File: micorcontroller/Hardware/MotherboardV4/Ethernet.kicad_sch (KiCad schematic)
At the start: 41 parts, among them IC2 W5500, J3 J1B1211CCD, Y1 ECS-250-6-33B2-CTP-TR

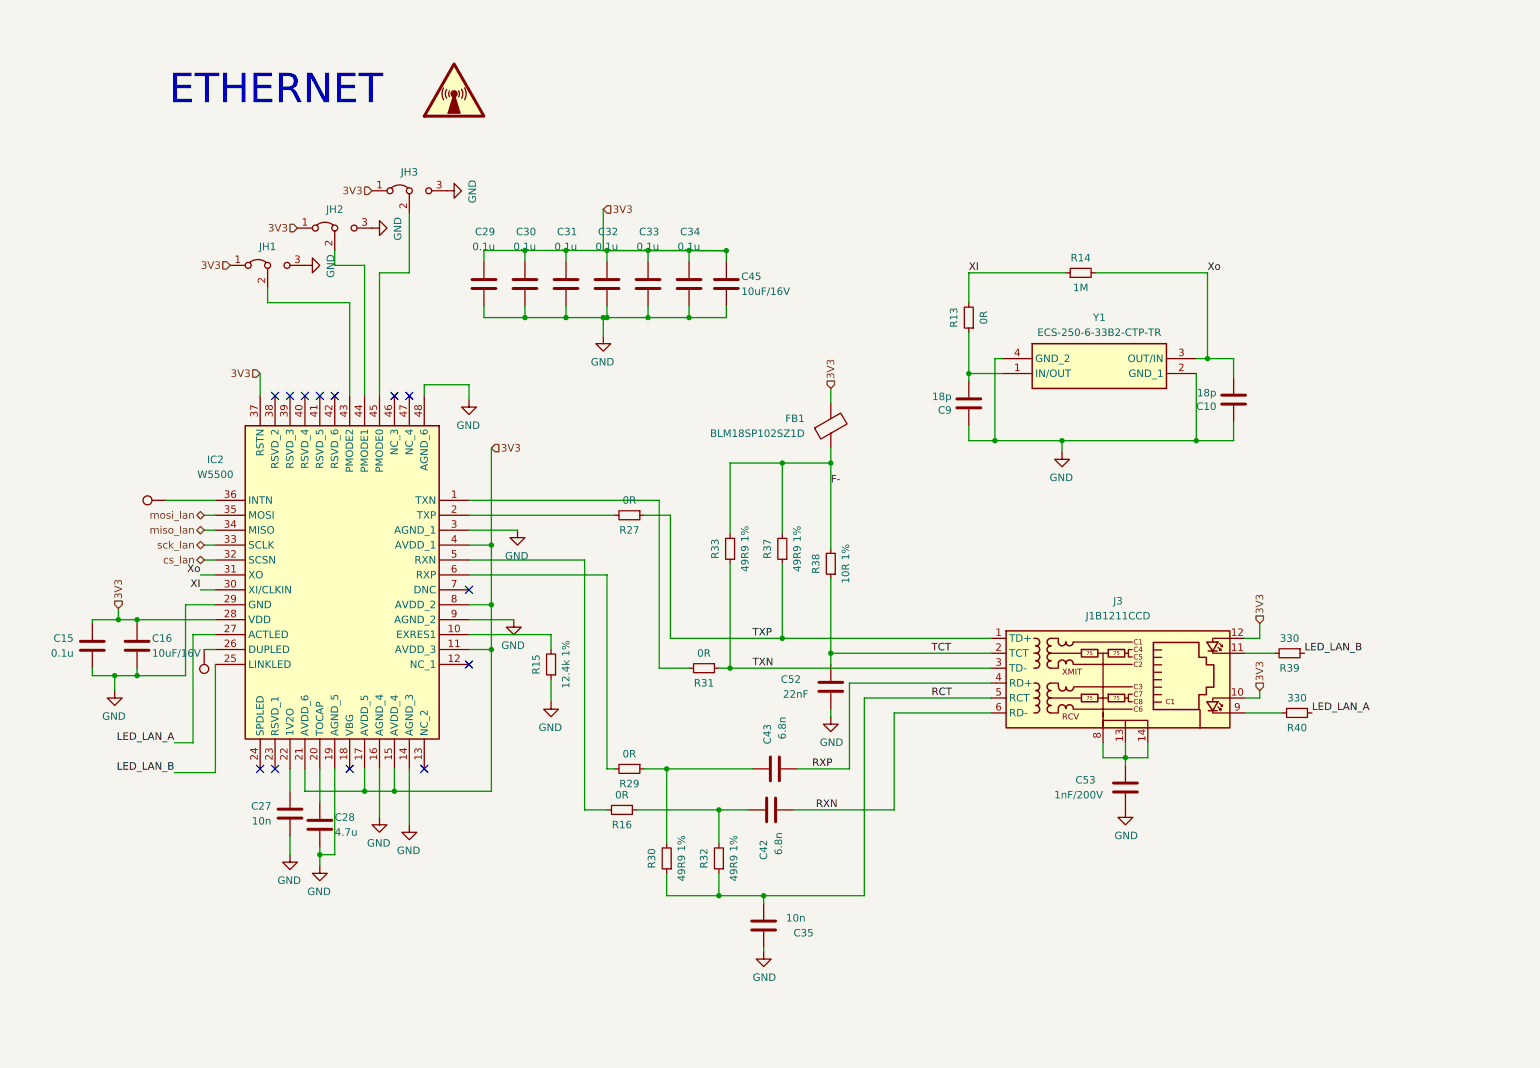
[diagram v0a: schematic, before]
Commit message: added NTC calculation
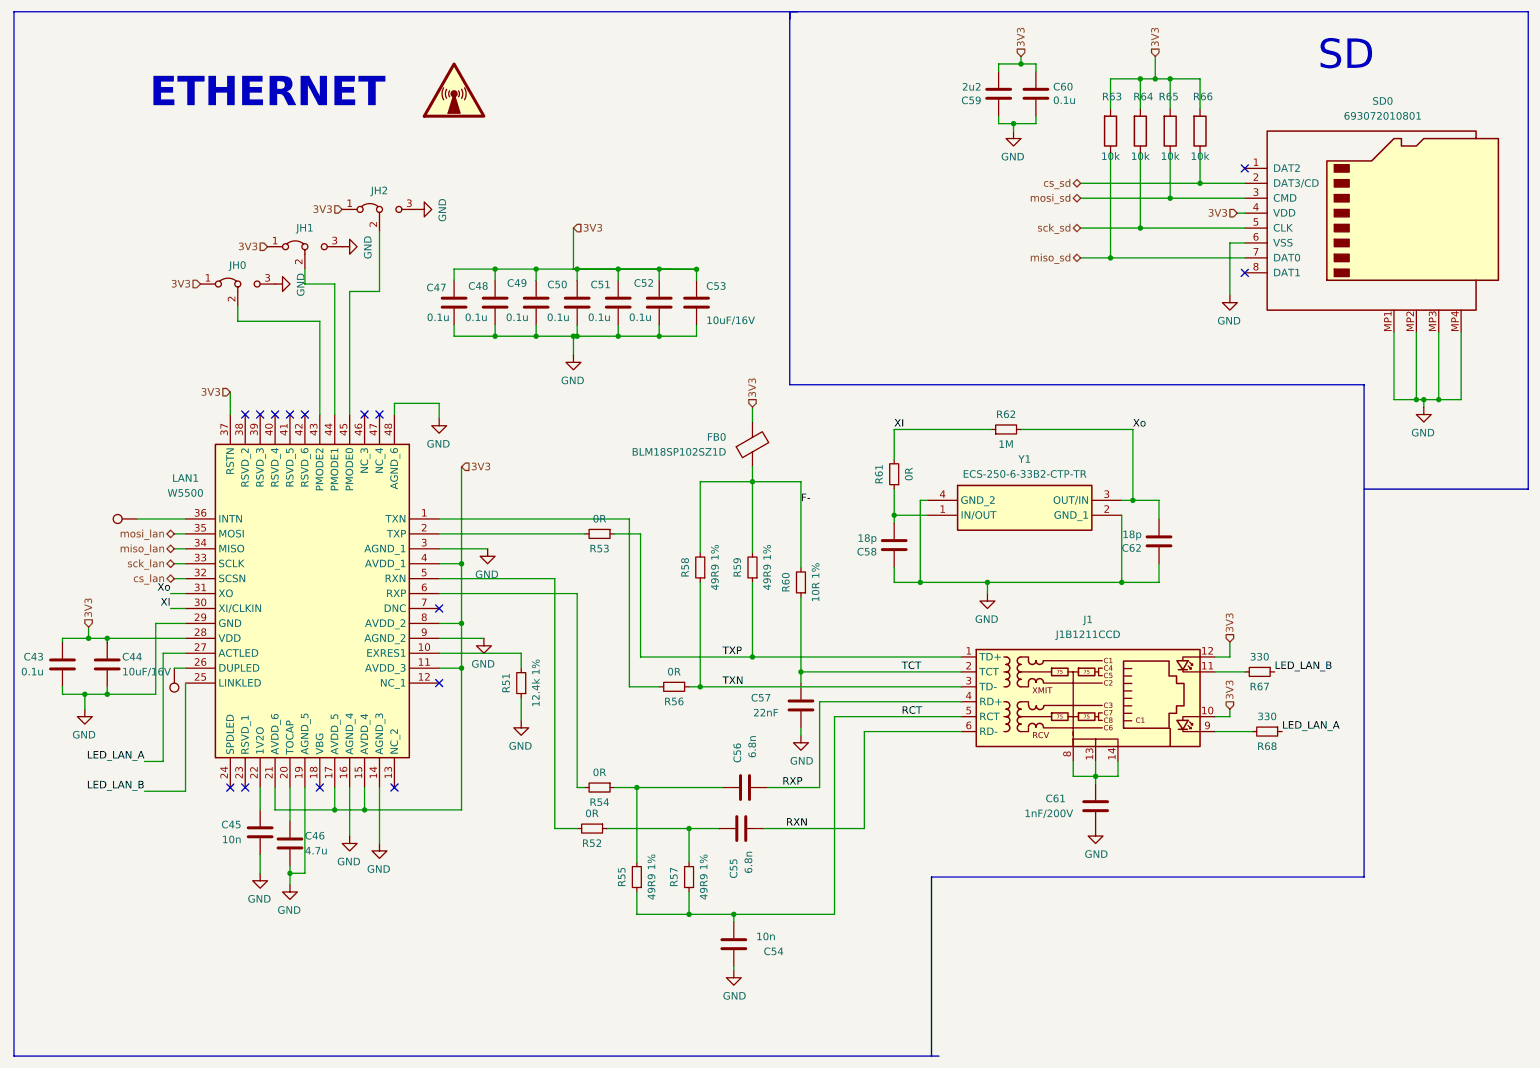
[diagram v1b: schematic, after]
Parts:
- added C59: 2u2, Capacitor_SMD:C_0805_2012Metric_Pad1.18x1.45mm_HandSolder, symbol Device:C
- added C60: 0.1u, Capacitor_SMD:C_0402_1005Metric_Pad0.74x0.62mm_HandSolder, symbol Device:C
- added R63, R64, R65, R66: 10k, Resistor_SMD:R_0603_1608Metric_Pad0.98x0.95mm_HandSolder, symbol Device:R
- added SD0: 693072010801, SamacSys_Parts:693072010801, symbol Connector:Micro_SD_Card
- renumbered C15 to C43, C16 to C44, C27 to C45, C28 to C46, C29 to C47, C30 to C48, C31 to C49, C32 to C50, C33 to C51, C34 to C52, C45 to C53, C35 to C54, C42 to C55, C43 to C56, C52 to C57, C9 to C58, C53 to C61, C10 to C62, FB1 to FB0, J3 to J1, JH1 to JH0, JH2 to JH1, JH3 to JH2, IC2 to LAN1, R15 to R51, R16 to R52, R27 to R53, R29 to R54, R30 to R55, R31 to R56, R32 to R57, R33 to R58, R37 to R59, R38 to R60, R13 to R61, R14 to R62, R39 to R67, R40 to R68, TP15 to TP3, TP16 to TP4
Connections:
- net 3V3: now also C59.2, C60.1, R63.2, R64.2, R65.2, R66.2, SD0.4 (VDD)
- net GND: now also C59.1, C60.2, SD0.6 (VSS), SD0.MP1, SD0.MP2, SD0.MP3, SD0.MP4
- new net cs_sd: R66.1, SD0.2 (DAT3/CD)
- new net miso_sd: R63.1, SD0.7 (DAT0)
- new net mosi_sd: R65.1, SD0.3 (CMD)
- new net sck_sd: R64.1, SD0.5 (CLK)
- no-connect marks 13 -> 15
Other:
- note added: "SD"
- moved on the sheet: C43, C44, C45, C46, C47, C48, C49, C50, C51, C52, C53, C54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

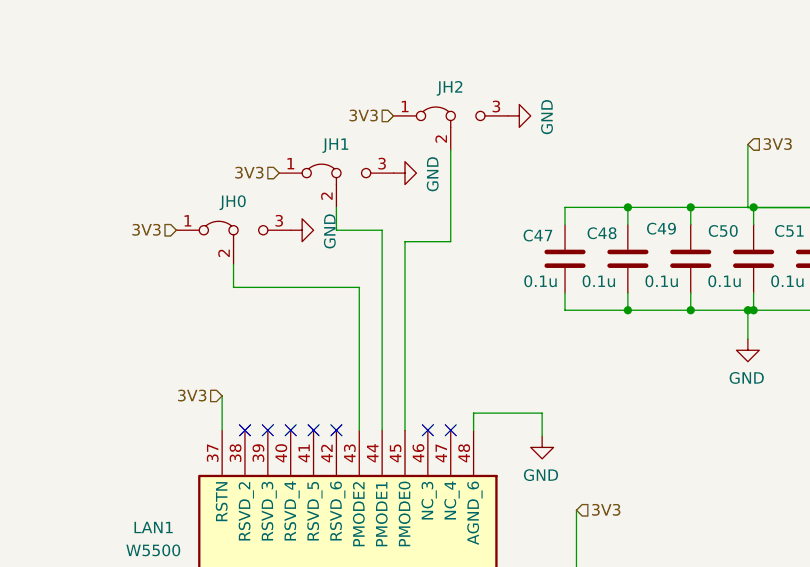
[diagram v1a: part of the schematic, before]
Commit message: added a serial command field for easy debugging
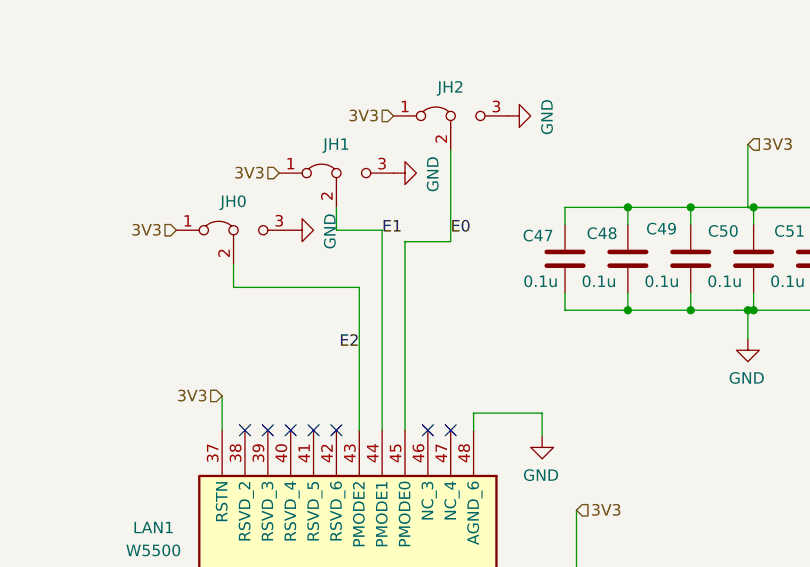
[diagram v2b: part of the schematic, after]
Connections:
- net E0: now reaches JH2.2 (C), LAN1.45 (PMODE0)
- net E2: now reaches JH0.2 (C), LAN1.43 (PMODE2)
- net E1: now reaches JH1.2 (C), LAN1.44 (PMODE1)
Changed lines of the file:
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@@
+		)
+	)
+	(label "E1"
+		(at 69.85 63.5 0)
+		(fields_autoplaced yes)
+		(effects
+			(font
+				(size 1.27 1.27)
+			)
+			(justify left bottom)
 		)
 	)
@@
 		)
 	)
+	(label "E2"
+		(at 67.31 76.2 180)
+		(fields_autoplaced yes)
+		(effects
+			(font
+				(size 1.27 1.27)
+			)
+			(justify right bottom)
+		)
+	)
 	(label "TCT"
 		(at 166.37 128.905 0)
@@
 		(fields_autoplaced yes)
 		(effects
+			(font
+				(size 1.27 1.27)
+			)
+			(justify left bottom)
+		)
+	)
+	(label "E0"
+		(at 77.47 63.5 0)
+		(fields_autoplaced yes)
+		(effects

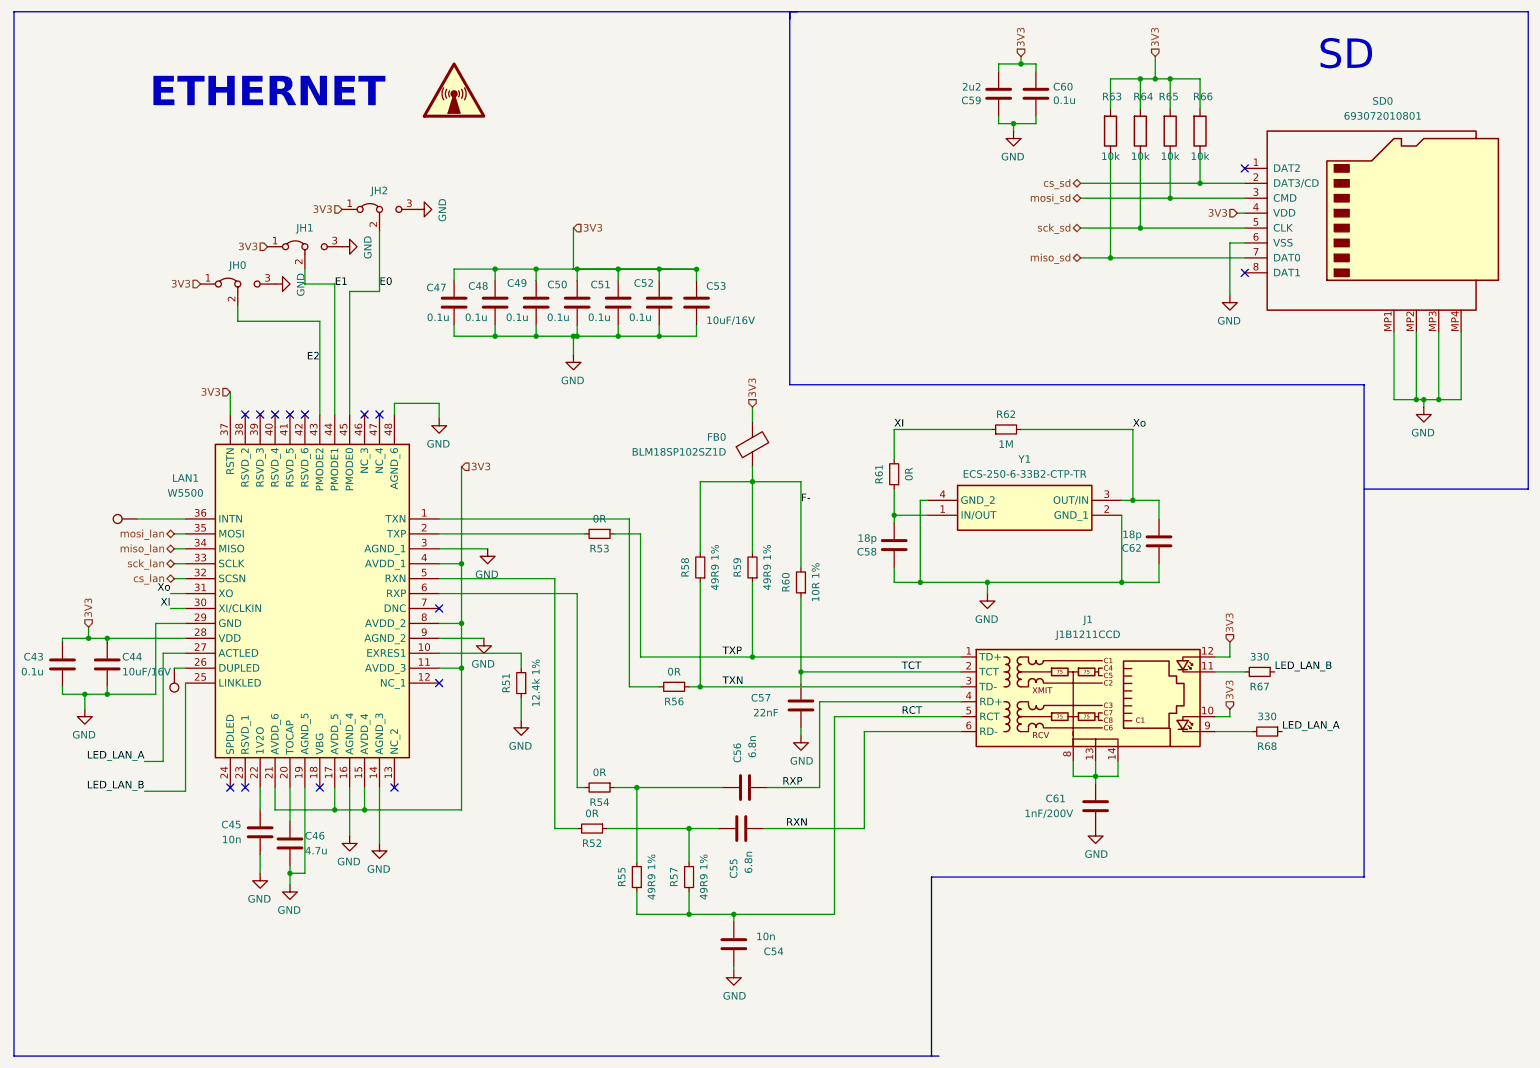
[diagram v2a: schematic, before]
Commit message: Switch to header BASED C file system {headache incomming}
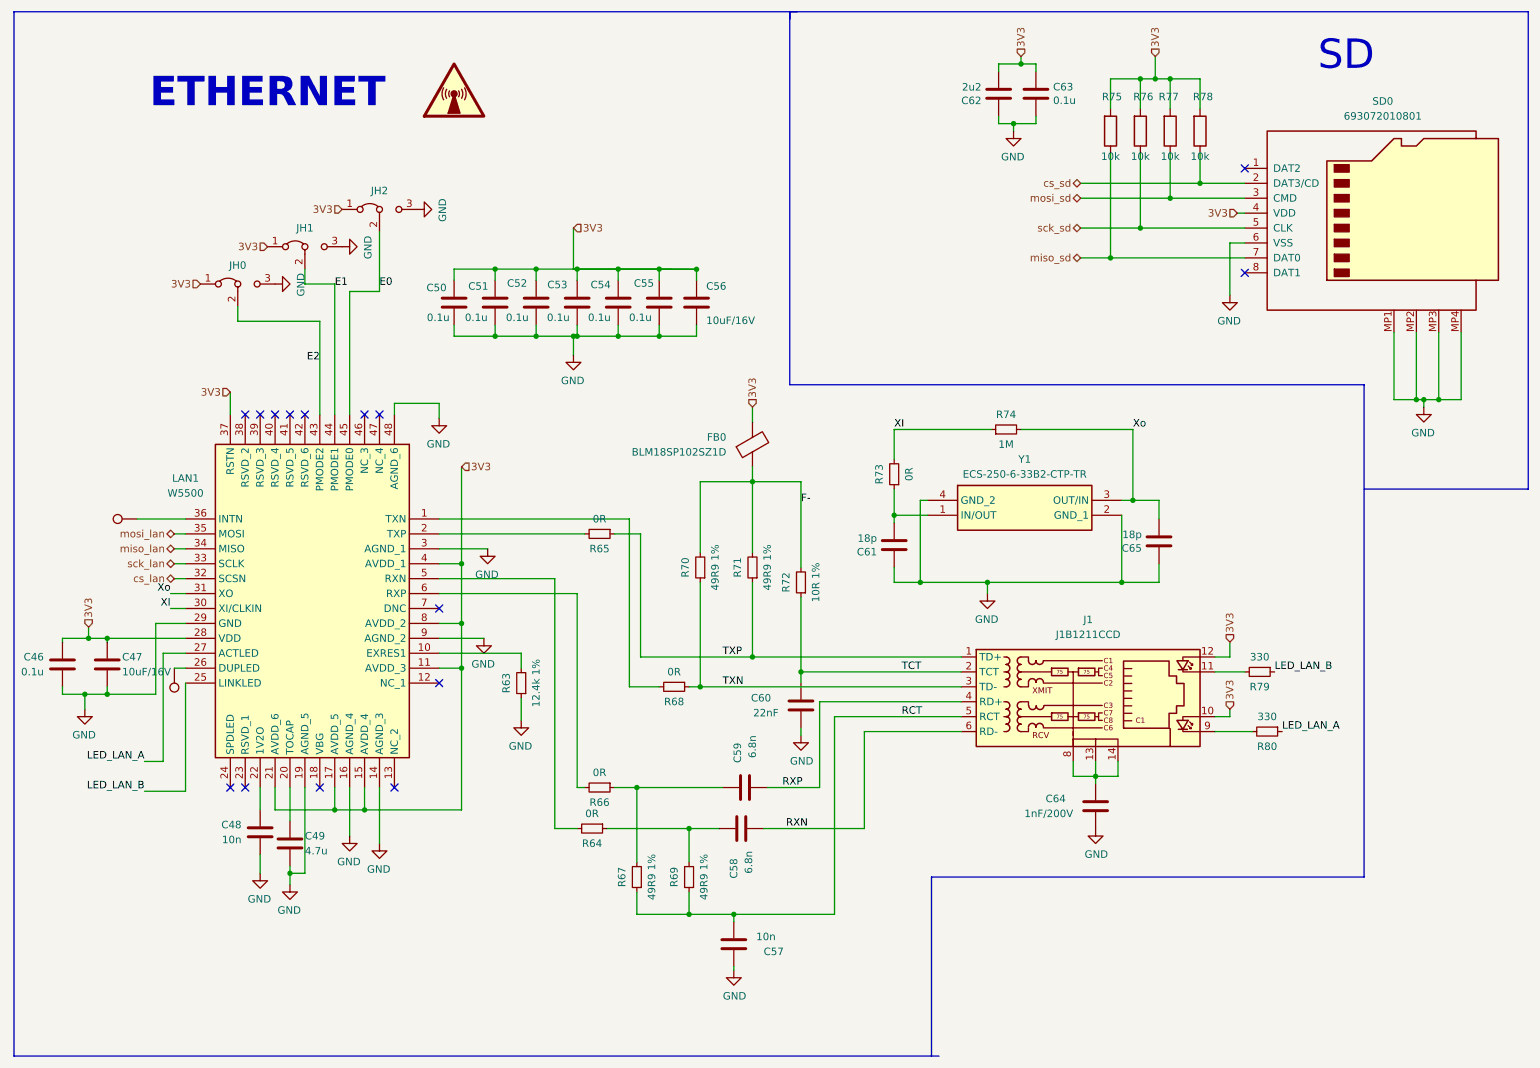
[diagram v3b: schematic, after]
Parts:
- renumbered C43 to C46, C44 to C47, C45 to C48, C46 to C49, C47 to C50, C48 to C51, C49 to C52, C50 to C53, C51 to C54, C52 to C55, C53 to C56, C54 to C57, C55 to C58, C56 to C59, C57 to C60, C58 to C61, C59 to C62, C60 to C63, C61 to C64, C62 to C65, R51 to R63, R52 to R64, R53 to R65, R54 to R66, R55 to R67, R56 to R68, R57 to R69, R58 to R70, R59 to R71, R60 to R72, R61 to R73, R62 to R74, R63 to R75, R64 to R76, R65 to R77, R66 to R78, R67 to R79, R68 to R80

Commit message: added uplink
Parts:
- C46, C47, C48, C49, C50, C51, C52, C53, C54, C55, C56, C57, C58, C59, C60, C61, C62, C63, C64, C65: symbol Device:C -> SymbolsBalloonv4:C
- FB0: symbol Device:FerriteBead -> SymbolsBalloonv4:FerriteBead
- J1: symbol Connector:RJ45_Wuerth_7499010121A -> SymbolsBalloonv4:RJ45_Wuerth_7499010121A
- JH0, JH1, JH2: symbol Jumper:Jumper_3_Bridged12 -> SymbolsBalloonv4:Jumper_3_Bridged12
- LAN1: symbol SamacSys_Parts:W5500 -> SymbolsBalloonv4:W5500
- R63, R64, R65, R66, R67, R68, R69, R70, R71, R72, R73, R74, R79, R80: symbol Device:R_Small -> SymbolsBalloonv4:R_Small
- R75, R76, R77, R78: symbol Device:R -> SymbolsBalloonv4:R
- SD0: symbol Connector:Micro_SD_Card -> SymbolsBalloonv4:Micro_SD_Card
- TP3, TP4: symbol Connector:TestPoint -> SymbolsBalloonv4:TestPoint
- Y1: symbol SamacSys_Parts:ECS-250-6-33B2-CTP-TR -> SymbolsBalloonv4:ECS-250-6-33B2-CTP-TR
